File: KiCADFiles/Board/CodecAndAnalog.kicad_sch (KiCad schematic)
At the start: 38 parts, among them J1 NCJ5FI-H, J2 NRJ4HF, J4 NRJ4HF, J5 NRJ4HF, SW4 LC2255EENPTAGBLK-ND, U302B1 OPA2348, U5 CS4272, X1 CRYSTAL

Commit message: chose all components
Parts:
- removed C33: 47uF, ~, symbol SuperAudioBoard-rescue:CP1
- removed U302B1: OPA2348, symbol SuperAudioBoard-rescue:OPA2348
- added C18: 100u, Capacitor_THT:CP_Radial_D5.0mm_P2.00mm, symbol Device:C_Small_US
- added U9: OPA1655D, Package_SO:SOIC-8_3.9x4.9mm_P1.27mm, symbol Amplifier_Operational:OPA1655D
- C19, C25, C30, C31, C32, C38: footprint ~ -> PCM_SparkFun-Capacitor:C_0603_1608Metric; MPN (none) -> CL10B104KB8NNNL
- C20, C28: value 10uF -> 10u; footprint ~ -> PCM_SparkFun-Capacitor:C_0805_2012Metric; MPN (none) -> CL21A106KAYNNNG; Voltage (none) -> 25V
- C21, C23, C34, C56: footprint (none) -> Capacitor_THT:CP_Radial_D5.0mm_P2.00mm; MPN (none) -> 25PX100MEFC5X11
- C26, C27: footprint ~ -> PCM_SparkFun-Capacitor:C_0603_1608Metric; MPN (none) -> KGM15ACG1E390JT
- C29: footprint ~ -> PCM_SparkFun-Capacitor:C_0603_1608Metric; MPN (none) -> CL10B105KP8NNNC
- FB3, FB4: footprint ~ -> Inductor_SMD:L_0603_1608Metric; MPN (none) -> MMZ1608B221CTAH0
- J1: MPN (none) -> NCJ5FI-H; now not fitted
- J2: MPN (none) -> NRJ4HF; now not fitted
- J4, J5: MPN (none) -> NRJ4HF
- R12, R30, R31, R34: footprint (none) -> PCM_SparkFun-Resistor:R_0805_2012Metric; MPN (none) -> CRCW0805100RFKEA
- R13: value 10 -> 34; footprint ~ -> PCM_SparkFun-Resistor:R_0805_2012Metric; MPN (none) -> CRCW080534R0FKEA
- R32, R33: footprint (none) -> PCM_SparkFun-Resistor:R_0805_2012Metric; MPN (none) -> RC0805FR-0747KL
- R5: footprint (none) -> PCM_SparkFun-Resistor:R_0805_2012Metric; MPN (none) -> ERA-6AEB3922V
- SW4: value LC2255EENPTAGBLK-ND -> ~; footprint (none) -> Connector_PinHeader_2.54mm:PinHeader_1x03_P2.54mm_Horizontal; MPN (none) -> LC2255EENPTAGBLK-ND
- TP3, TP4, TP5, TP6: footprint (none) -> TestPoint:TestPoint_2Pads_Pitch2.54mm_Drill0.8mm; now not fitted
- U5: footprint ~ -> Package_SO:TSSOP-28-1EP_4.4x9.7mm_P0.65mm_EP2.74x4.75mm; MPN (none) -> CS4272; now not fitted
- X1: value CRYSTAL -> 24.576 MHz 20 pF; footprint ~ -> Crystal:Crystal_SMD_3225-4Pin_3.2x2.5mm_HandSoldering; MFG1 PN ECS-245.7-20-5PX-TR -> ECS-245.7-20-5PX-TR; MPN (none) -> ECS-245.7-20-5PX-TR
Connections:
- net +5VA: now also U9.7 (V+)
- net GND: now also C18.2, U9.4 (V-)
- net VCOM: now also U9.3 (+)
- net at C32.1, U5.22 (FILT): now also C18.1
- net at R13.2: now also U9.2 (-), U9.6
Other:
- moved on the sheet: R12, X1

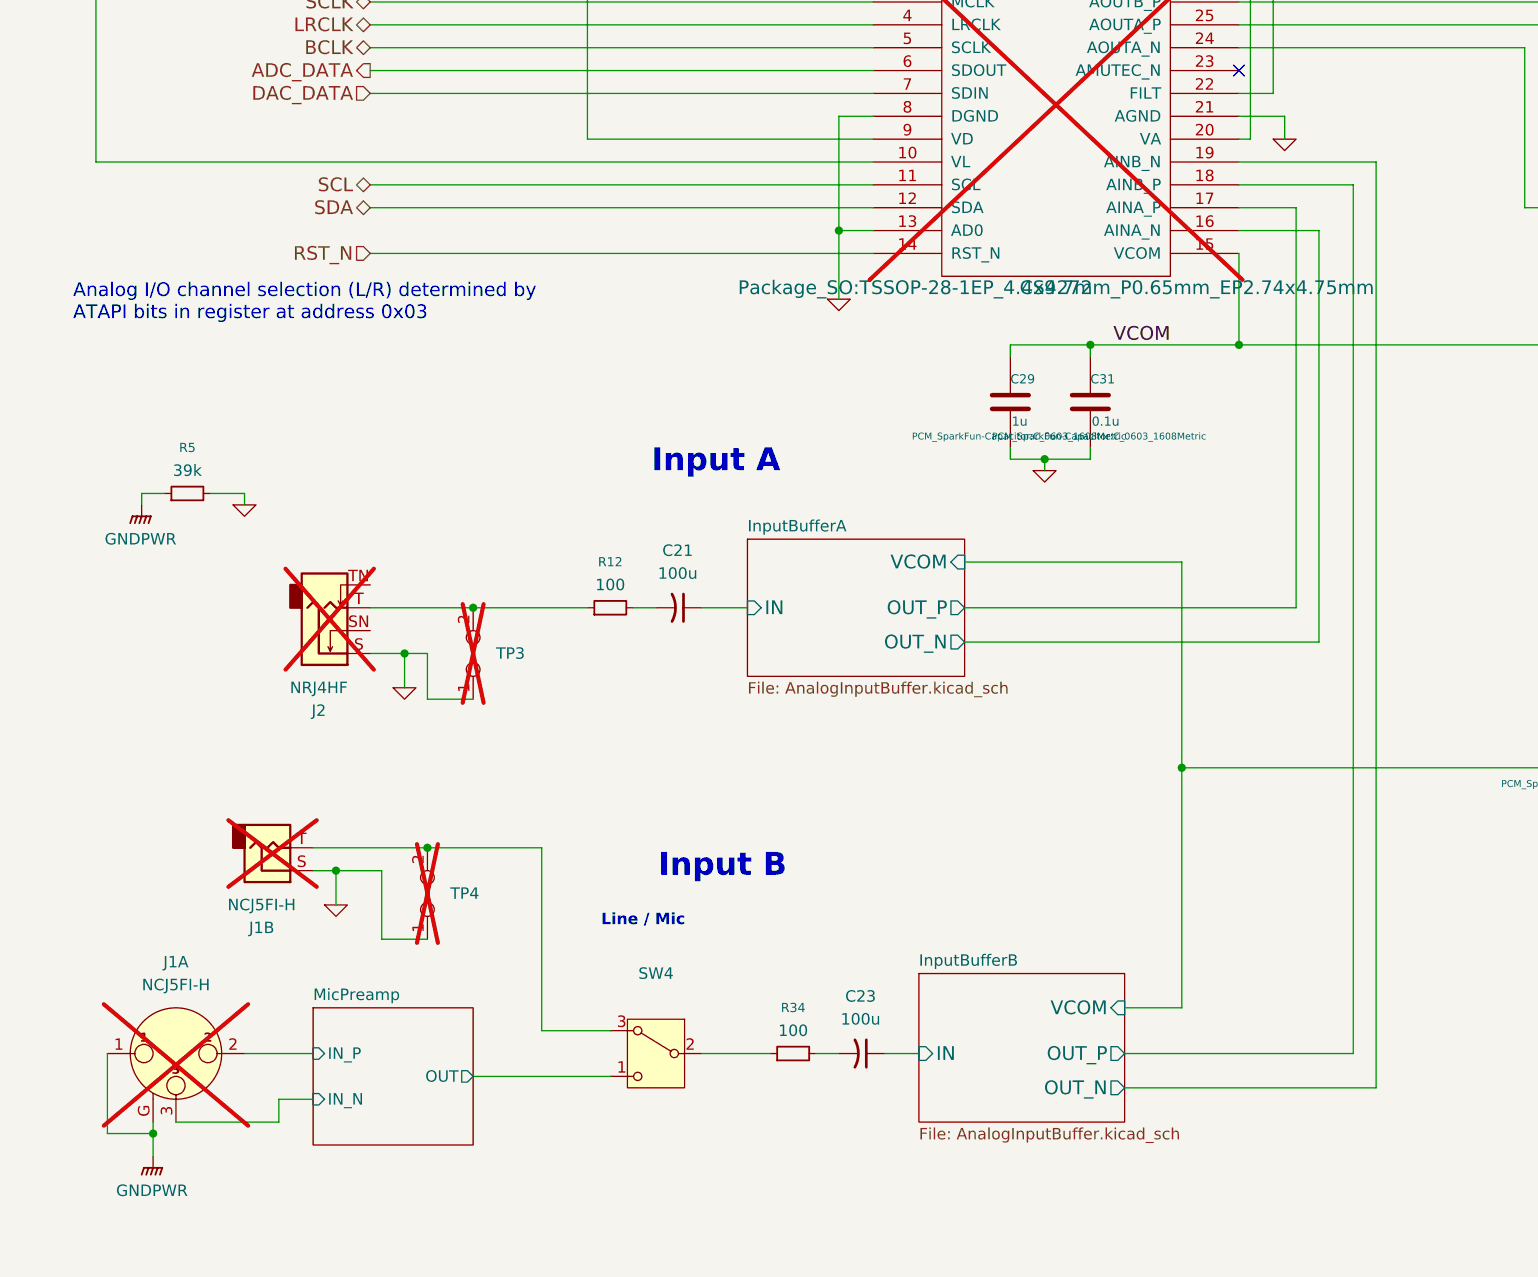
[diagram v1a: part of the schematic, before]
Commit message: replaced sw with relay, routed line amp section
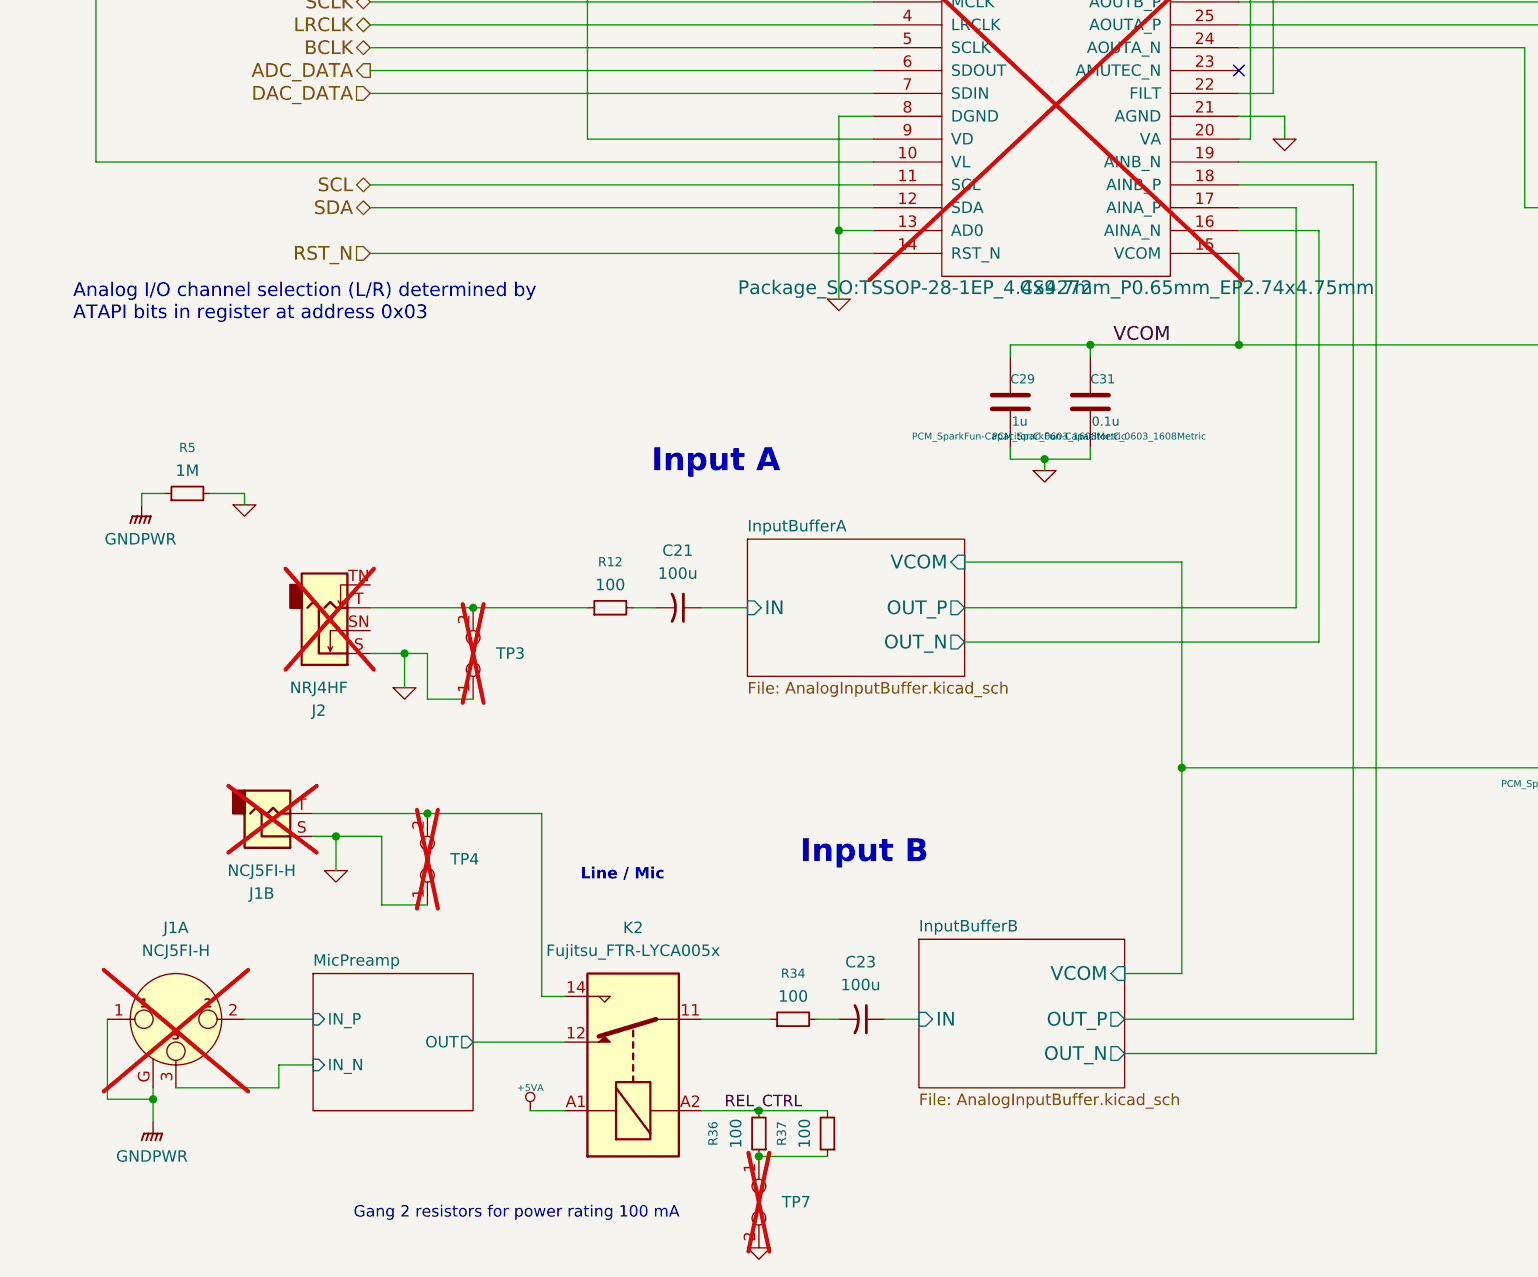
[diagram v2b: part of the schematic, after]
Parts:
- removed SW4: ~, Connector_PinHeader_2.54mm:PinHeader_1x03_P2.54mm_Horizontal, symbol Switch:SW_SPDT_321
- added K2: Fujitsu_FTR-LYCA005x, Relay_THT:Relay_SPDT_Fujitsu_FTR-LYCA005x_FormC_Vertical, symbol Relay:Fujitsu_FTR-LYCA005x
- added R36, R37: 100, PCM_SparkFun-Resistor:R_0805_2012Metric, symbol Device:R_Small
- added TP7: TestPoint_2Pole, TestPoint:TestPoint_2Pads_Pitch2.54mm_Drill0.8mm, symbol Connector:TestPoint_2Pole
- R5: value 39k -> 1M; MPN ERA-6AEB3922V -> (none)
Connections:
- net +5VA: now also K2.A1
- net GND: now also TP7.2
- net MicPreamp/OUT: now also K2.12
- net at J1.T, TP4.2: now also K2.14
- net at R34.1: now also K2.11
- new net: R36.1, R37.1, TP7.1
- new net REL_CTRL: K2.A2, R36.2, R37.2
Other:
- note added: "Gang 2 resistors for power rating 100 mA"
- moved on the sheet: C23, J1A, J1B, R34, TP4

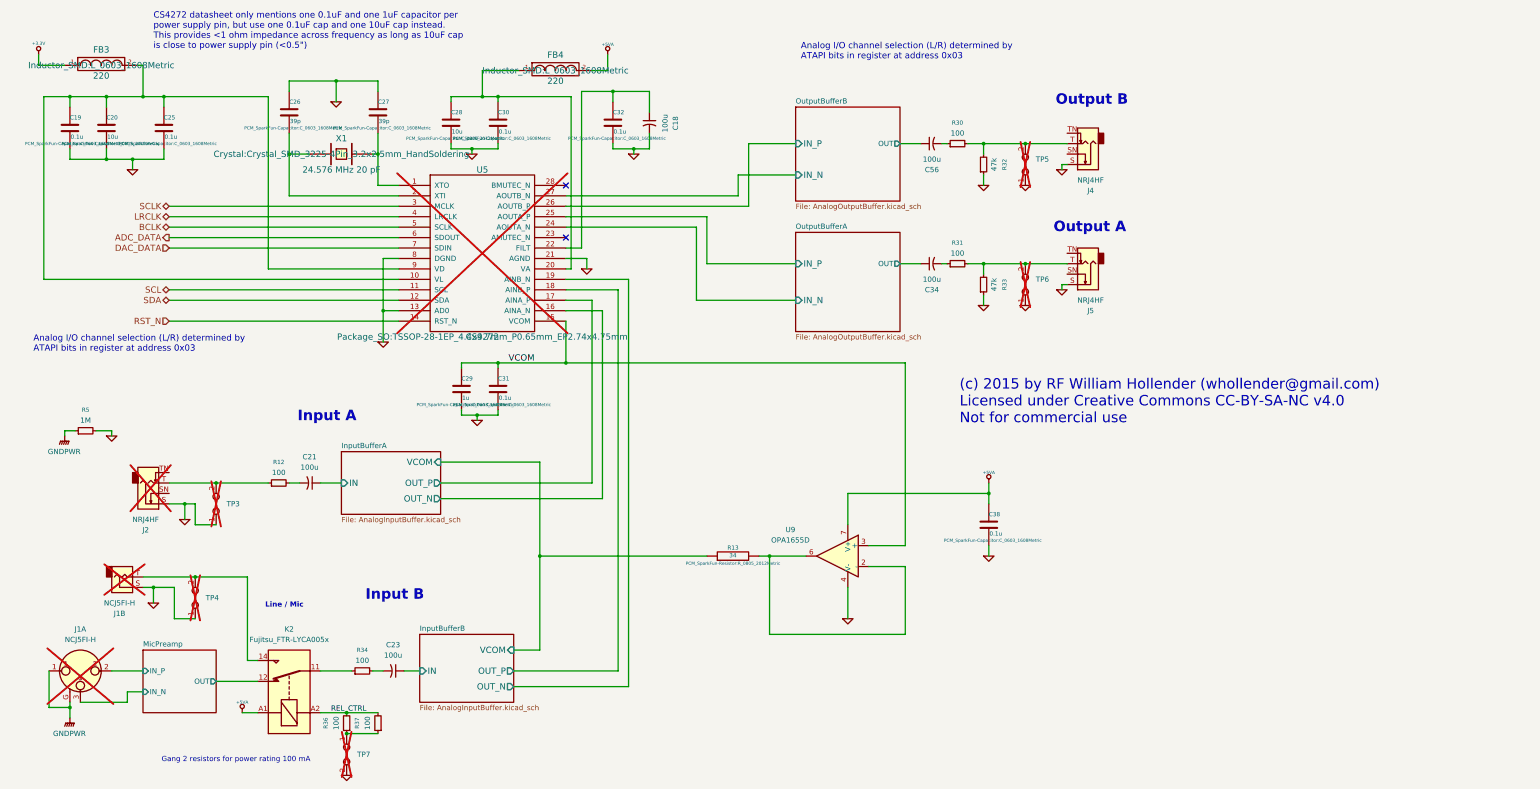
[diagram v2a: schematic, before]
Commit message: removed connectors and condensed layout
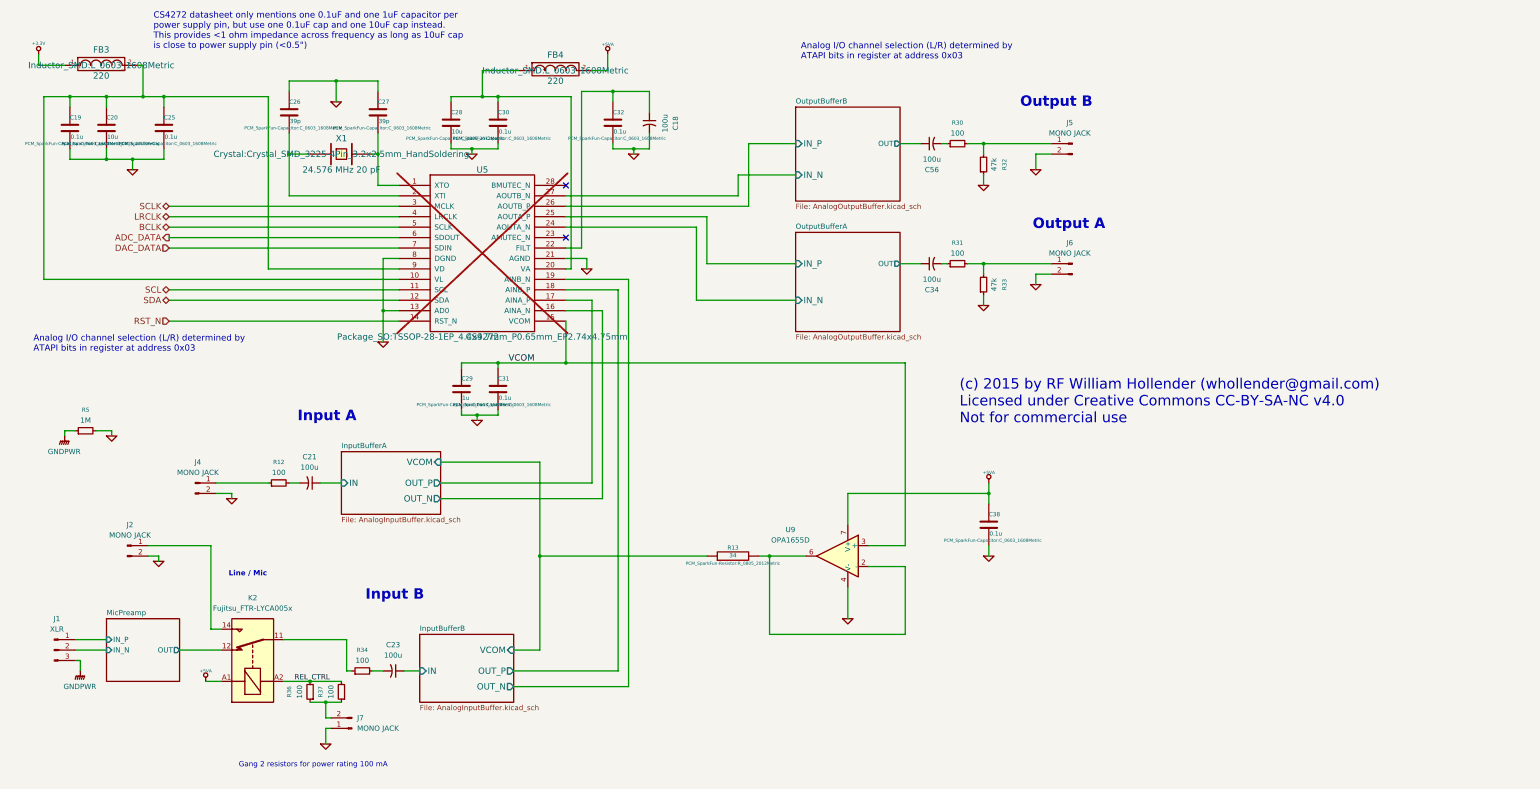
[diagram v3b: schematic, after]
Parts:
- removed J1: NCJ5FI-H, Connector_Audio:Jack_XLR-6.35mm_Neutrik_NCJ5FI-H_Horizontal, symbol Connector_Audio:NCJ5FI-H
- removed J2, J4, J5: NRJ4HF, Connector_Audio:Jack_6.35mm_Neutrik_NRJ4HF_Horizontal, symbol Connector_Audio:NRJ4HF
- removed TP3, TP4, TP5, TP6, TP7: TestPoint_2Pole, TestPoint:TestPoint_2Pads_Pitch2.54mm_Drill0.8mm, symbol Connector:TestPoint_2Pole
- added J1: XLR, Connector_PinHeader_2.54mm:PinHeader_1x03_P2.54mm_Vertical, symbol Connector:Conn_01x03_Pin
- added J2, J4, J5, J6, J7: MONO JACK, Connector_PinHeader_2.54mm:PinHeader_1x02_P2.54mm_Vertical, symbol Connector:Conn_01x02_Pin
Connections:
- net GND: now also J2.2 (Pin_2), J4.2 (Pin_2), J5.2 (Pin_2), J6.2 (Pin_2), J7.1 (Pin_1)
- net GNDPWR: now also J1.3 (Pin_3)
- net MicPreamp/IN_N: now also J1.2 (Pin_2)
- net MicPreamp/IN_P: now also J1.1 (Pin_1)
- net at R30.2, R32.2: now also J5.1 (Pin_1)
- net at K2.14: now also J2.1 (Pin_1)
- net at R31.2, R33.2: now also J6.1 (Pin_1)
- net at R36.1, R37.1: now also J7.2 (Pin_2)
- net at R12.1: now also J4.1 (Pin_1)
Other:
- moved on the sheet: K2, R36, R37

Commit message: improved layout further
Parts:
- removed C19: 0.1u, PCM_SparkFun-Capacitor:C_0603_1608Metric, symbol SuperAudioBoard-rescue:C
- U5: footprint Package_SO:TSSOP-28-1EP_4.4x9.7mm_P0.65mm_EP2.74x4.75mm -> Package_SO:TSSOP-28_4.4x9.7mm_P0.65mm; now fitted
- X1: footprint Crystal:Crystal_SMD_3225-4Pin_3.2x2.5mm_HandSoldering -> Crystal:Crystal_SMD_HC49-SD_HandSoldering
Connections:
- net VD_FILT: now reaches C20.1, C25.1, FB3.2, U5.10 (VL), U5.9 (VD)
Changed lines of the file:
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@@
 	)
 	(junction
-		(at 25.4 29.21)
-		(diameter 0)
-		(color 0 0 0 0)
-	)
-	(junction
 		(at 129.54 93.98)
 		(diameter 0)
@@
 	)
 	(junction
-		(at 34.29 44.45)
-		(diameter 0)
-		(color 0 0 0 0)
-	)
-	(junction
 		(at 195.58 140.97)
 		(diameter 0)
@@
 	(wire
 		(pts
-			(xy 25.4 44.45) (xy 25.4 41.91)
-		)
-		(stroke
-			(width 0)
-			(type default)
-		)
-	)
-	(wire
-		(pts
 			(xy 134.62 22.86) (xy 125.73 22.86)
 		)
@@
 	(wire
 		(pts
-			(xy 25.4 44.45) (xy 34.29 44.45)
-		)
-		(stroke
-			(width 0)
-			(type default)
-		)
-	)
-	(wire
-		(pts
 			(xy 133.35 168.91) (xy 158.75 168.91)
 		)
@@
 	(wire
 		(pts
-			(xy 25.4 29.21) (xy 19.05 29.21)
+			(xy 19.05 29.21) (xy 34.29 29.21)
 		)
 		(stroke
@@
 	(wire
 		(pts
-			(xy 34.29 29.21) (xy 25.4 29.21)
-		)
-		(stroke
-			(width 0)
-			(type default)
-		)
-	)
-	(wire
-		(pts
 			(xy 49.53 58.42) (xy 105.41 58.42)
 		)
@@
 	(wire
 		(pts
-			(xy 25.4 29.21) (xy 25.4 31.75)
-		)
-		(stroke
-			(width 0)
-			(type default)
-		)
-	)
-	(wire
-		(pts
 			(xy 133.35 172.72) (xy 161.29 172.72)
 		)
@@
 		)
 	)
+	(label "VD_FILT"
+		(at 53.34 29.21 0)
+		(effects
+			(font
+				(size 1.27 1.27)
+			)
+			(justify left bottom)
+		)
+	)
 	(label "VCOM"
 		(at 138.43 93.98 180)
@@
 		(in_bom yes)
 		(on_board yes)
-		(dnp yes)
+		(dnp no)
 		(property "Reference" "U5"
 			(at 125.73 46.99 0)
@@
 			)
 		)
-		(property "Footprint" "Package_SO:TSSOP-28-1EP_4.4x9.7mm_P0.65mm_EP2.74x4.75mm"
+		(property "Footprint" "Package_SO:TSSOP-28_4.4x9.7mm_P0.65mm"
 			(at 125.73 87.63 0)
 			(effects
@@
 			)
 		)
-		(property "Datasheet" "~"
+		(property "Datasheet" "https://statics.cirrus.com/pubs/proDatasheet/CS4272_F2.pdf"
 			(at 125.73 87.63 0)
 			(effects
@@
 			)
 		)
-		(property "Footprint" "Crystal:Crystal_SMD_3225-4Pin_3.2x2.5mm_HandSoldering"
+		(property "Footprint" "Crystal:Crystal_SMD_HC49-SD_HandSoldering"
 			(at 91.44 43.18 0)
 			(effects
@@
 					(unit 1)
 				)
-			)
-		)
-	)
-	(symbol
-		(lib_name "C_19")
-		(lib_id "SuperAudioBoard-rescue:C")
-		(at 25.4 36.83 0)
-		(unit 1)
-		(exclude_from_sim no)
-		(in_bom yes)
-		(on_board yes)
-		(dnp no)
-		(property "Reference" "C19"
-			(at 25.4 34.29 0)
-			(effects
-				(font
-					(size 1.016 1.016)
-				)
-				(justify left)
-			)
-		)
-		(property "Value" "0.1u"
-			(at 25.5524 38.989 0)
-			(effects
-				(font
-					(size 1.016 1.016)
-				)
-				(justify left)
-			)
-		)
-		(property "Footprint" "PCM_SparkFun-Capacitor:C_0603_1608Metric"
-			(at 26.3652 40.64 0)
-			(effects
-				(font
-					(size 0.762 0.762)
-				)
-			)
-		)
-		(property "Datasheet" "~"
-			(at 25.4 36.83 0)
-			(effects
-				(font
-					(size 1.524 1.524)
-				)
-			)
-		)
-		(property "Description" ""
-			(at 25.4 36.83 0)
-			(effects
-				(font
-					(size 1.27 1.27)
-				)
-			)
-		)
-		(property "MFG 1 Name" "Murata"
-			(at 25.4 36.83 0)
-			(effects
-				(font
-					(size 1.524 1.524)
-				)
-				(hide yes)
-			)
-		)
-		(property "MFG1 PN" "GRM188R71E104KA01"
-			(at 25.4 36.83 0)
-			(effects
-				(font
-					(size 1.524 1.524)
-				)
-				(hide yes)
-			)
-		)
-		(property "MFG 2 Name" "TDK"
-			(at 25.4 36.83 0)
-			(effects
-				(font
-					(size 1.524 1.524)
-				)
-				(hide yes)
-			)
-		)
-		(property "MFG 2 PN" "C1608X7R1E104K080AA"
-			(at 25.4 36.83 0)
-			(effects
-				(font
-					(size 1.524 1.524)
-				)
-				(hide yes)
-			)
-		)
-		(property "MPN" "CL10B104KB8NNNL"
-			(at 25.4 36.83 0)
-			(effects
-				(font
-					(size 1.27 1.27)
-				)
-				(hide yes)
-			)
-		)
-		(property "Tol" ""
-			(at 25.4 36.83 0)
-			(effects
-				(font
-					(size 1.27 1.27)
-				)
-				(hide yes)
-			)
-		)
-		(pin "1"
-		)
-		(pin "2"
-		)
-		(instances
-			(project "SuperAudioBoard"
-				(path "/01f65e03-4e05-4001-87b4-b3e88e4198ab/00000000-0000-0000-0000-00005438c479"
-					(reference "C19")
-					(unit 1)
-				)

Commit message: made crystal footprint smaller
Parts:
- X1: MFG 2 PN 9C-24.576MBBK-T -> ABM3-24.576MHZ-B2-T; MFG1 PN ECS-245.7-20-5PX-TR -> ABM3-24.576MHZ-B2-T; MPN ECS-245.7-20-5PX-TR -> ABM3-24.576MHZ-B2-T
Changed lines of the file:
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@@
 			)
 		)
-		(property "MFG1 PN" "ECS-245.7-20-5PX-TR "
+		(property "MFG1 PN" "ABM3-24.576MHZ-B2-T "
 			(at 91.44 43.18 0)
 			(effects
@@
 			)
 		)
-		(property "MFG 2 PN" "9C-24.576MBBK-T"
+		(property "MFG 2 PN" "ABM3-24.576MHZ-B2-T "
 			(at 91.44 43.18 0)
 			(effects
@@
 			)
 		)
-		(property "MPN" "ECS-245.7-20-5PX-TR "
+		(property "MPN" "ABM3-24.576MHZ-B2-T "
 			(at 91.44 43.18 0)
 			(effects
